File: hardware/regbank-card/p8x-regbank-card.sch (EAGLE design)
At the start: 45 parts, among them J1 DIN41612-96M, U1 P0 L0, U10 P2 L1, U11 P2 H0, U12 P2 H1, U13 P3 L0, U14 P3 L1, U15 P3 H0, U16 P3 H1, U17 PTR SEL 0, U18 PTR SEL 1, U19 PTR SEL 2, U2 P0 L1, U20 PTR SEL 3, U21 PTR SEL 4, U22 PTR SEL 5, U23 PTR SEL 6, U24 PTR SEL 7, U25 ADDR LO, U26 ADDR HI, U27 RDBK LO, U28 RDBK HI, U29 RDBK OUT, U3 P0 H0, U30 DLD DEC, U31 DOE DEC, U32 LOAD DEC, U33 SEL+CNT DEC, U34 74HCT02, U35 74HCT14, U36 ZERO P0, U37 74HCT08, U38 74HCT08, U4 P0 H1, U5 P1 L0, U6 P1 L1, U7 P1 H0, U8 P1 H1, U9 P2 L0

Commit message: hw(rev B): reg-bank — 3-bit PSEL decode + PT scratch pointer
Phase 2, step 3. Select decode U33 becomes a 74138 (3-bit PSEL -> -SEL0..4,
so PSEL=4 no longer aliases to P0); count decode moves to a new 74139
(U39, P0-P3 only). U40 (74HCT32) gates the P0-P3 load decoder off when
PSEL2=1 and derives the PT load strobes (-LDL4 = -LDL|-SEL4, etc.). PT
itself is two 74377 latches (U41/U42) loaded from D0-7, driven onto the
pointer bus by two 74244 buffers (U43/U44) when -SEL4 — so it reaches the
address bus and readback path like any pointer. Card retitled REV B.
Validates clean (pin/pad level; not yet electrically DRC'd).

Co-Authored-By: Claude Opus 4.8 <noreply@anthropic.com>
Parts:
- added U39: CNT DEC, p8x:74139
- added U40: 74HCT32, p8x:GATES14
- added U41: PT LO, p8x:74377V2
- added U42: PT HI, p8x:74377V2
- added U43: PT SEL LO, p8x:74244
- added U44: PT SEL HI, p8x:74244
- U33: value SEL+CNT DEC -> SEL DEC; device p8x:74139 -> p8x:74138
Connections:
- new net -LDH4: U40.4Y, U42.!E
- new net -LDHG: U32.!G2, U40.2Y
- new net -LDL4: U40.3Y, U41.!E
- new net -LDLG: U32.!G1, U40.1Y
- new net -SEL4: U33.Y4, U40.3B, U40.4B, U43.!G1, U43.!G2, U44.!G1, U44.!G2
- new net PSEL2: J1.C27, U33.C, U40.1B, U40.2B
- new net PTQ0_0: U41.Q1, U43.A1
- new net PTQ0_1: U41.Q2, U43.A2
- new net PTQ0_2: U41.Q3, U43.A3
- new net PTQ0_3: U41.Q4, U43.A4
- new net PTQ0_4: U41.Q5, U43.A5
- new net PTQ0_5: U41.Q6, U43.A6
- new net PTQ0_6: U41.Q7, U43.A7
- new net PTQ0_7: U41.Q8, U43.A8
- new net PTQ1_0: U42.Q1, U44.A1
- new net PTQ1_1: U42.Q2, U44.A2
- new net PTQ1_2: U42.Q3, U44.A3
- new net PTQ1_3: U42.Q4, U44.A4
- new net PTQ1_4: U42.Q5, U44.A5
- new net PTQ1_5: U42.Q6, U44.A6
- new net PTQ1_6: U42.Q7, U44.A7
- new net PTQ1_7: U42.Q8, U44.A8
- net -CNT0: now also U39.1Y0; no longer U33.2Y0
- net -CNT1: now also U39.1Y1; no longer U33.2Y1
- net -CNT2: now also U39.1Y2; no longer U33.2Y2
- net -CNT3: now also U39.1Y3; no longer U33.2Y3
- net -LDH: now also U40.2A, U40.4A; no longer U32.!G2
- net -LDL: now also U40.1A, U40.3A; no longer U32.!G1
- net -SEL0: now also U33.Y0; no longer U33.1Y0
- net -SEL1: now also U33.Y1; no longer U33.1Y1
- net -SEL2: now also U33.Y2; no longer U33.1Y2
- net -SEL3: now also U33.Y3; no longer U33.1Y3
- net CLK: now also U41.CLK, U42.CLK
- net CNTN: now also U39.!G1; no longer U33.!G2
- net D0: now also U41.D1, U42.D1
- net D1: now also U41.D2, U42.D2
- net D2: now also U41.D3, U42.D3
- net D3: now also U41.D4, U42.D4
- net D4: now also U41.D5, U42.D5
- net D5: now also U41.D6, U42.D6
- net D6: now also U41.D7, U42.D7
- net D7: now also U41.D8, U42.D8
- net GND: now also U33.!G2A, U33.!G2B, U39.A2, U39.B2; no longer U33.!G1
- net PB0: now also U43.Y1
- net PB1: now also U43.Y2
- net PB10: now also U44.Y3
- net PB11: now also U44.Y4
- net PB12: now also U44.Y5
- net PB13: now also U44.Y6
- net PB14: now also U44.Y7
- net PB15: now also U44.Y8
- net PB2: now also U43.Y3
- net PB3: now also U43.Y4
- net PB4: now also U43.Y5
- net PB5: now also U43.Y6
- net PB6: now also U43.Y7
- net PB7: now also U43.Y8
- net PB8: now also U44.Y1
- net PB9: now also U44.Y2
- net PSEL0: now also U33.A, U39.A1; no longer U33.A1, U33.A2
- net PSEL1: now also U33.B, U39.B1; no longer U33.B1, U33.B2
- net VCC: now also U33.G1, U39.!G2
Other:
- note added: "P8X REGISTER BANK CARD REV B (P0=PC P3=SP, PT scratch)"
- note removed: "P8X REGISTER BANK CARD REV A (P0=PC P3=SP)"
- moved on the sheet: LED3, LED4, LED5, R4, R5, RP1

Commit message: hw: per-IC 100nF decoupling caps on every card
card standards sec.5 requires a decoupling cap per IC; only the backplane had
them. gen_eagle's card() now generates one 100nF cap (CDn, C_DISC footprint)
per IC on the five plug-in cards, placed next to its IC and wired VCC<->GND;
the memory card's separate build does the same for U1-U9.

Caps added: control 18, regbank 44, alu 31, io 15, cf 8, memory 9. All 7
boards regenerate with 0 validation errors; card schematic PDFs refreshed.
Placement is approximate (caps sit just below each IC) pending Fusion routing.

Clears a pre-fab blocker from the backlog.

Co-Authored-By: Claude Opus 4.8 <noreply@anthropic.com>
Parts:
- added CD1, CD10, CD11, CD12, CD13, CD14, CD15, CD16, CD17, CD18, CD19, CD2, CD20, CD21, CD22, CD23, CD24, CD25, CD26, CD27, CD28, CD29, CD3, CD30, CD31, CD32, CD33, CD34, CD35, CD36, CD37, CD38, CD39, CD4, CD40, CD41, CD42, CD43, CD44, CD5, CD6, CD7, CD8, CD9: 100N, p8x:CAP
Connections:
- net GND: now also CD1.2, CD10.2, CD11.2, CD12.2, CD13.2, CD14.2, CD15.2, CD16.2, CD17.2, CD18.2, CD19.2, CD2.2, CD20.2, CD21.2, CD22.2, CD23.2, CD24.2, CD25.2, CD26.2, CD27.2, CD28.2, CD29.2, CD3.2, CD30.2, CD31.2, CD32.2, CD33.2, CD34.2, CD35.2, CD36.2, CD37.2, CD38.2, CD39.2, CD4.2, CD40.2, CD41.2, CD42.2, CD43.2, CD44.2, CD5.2, CD6.2, CD7.2, CD8.2, CD9.2
- net VCC: now also CD1.1, CD10.1, CD11.1, CD12.1, CD13.1, CD14.1, CD15.1, CD16.1, CD17.1, CD18.1, CD19.1, CD2.1, CD20.1, CD21.1, CD22.1, CD23.1, CD24.1, CD25.1, CD26.1, CD27.1, CD28.1, CD29.1, CD3.1, CD30.1, CD31.1, CD32.1, CD33.1, CD34.1, CD35.1, CD36.1, CD37.1, CD38.1, CD39.1, CD4.1, CD40.1, CD41.1, CD42.1, CD43.1, CD44.1, CD5.1, CD6.1, CD7.1, CD8.1, CD9.1

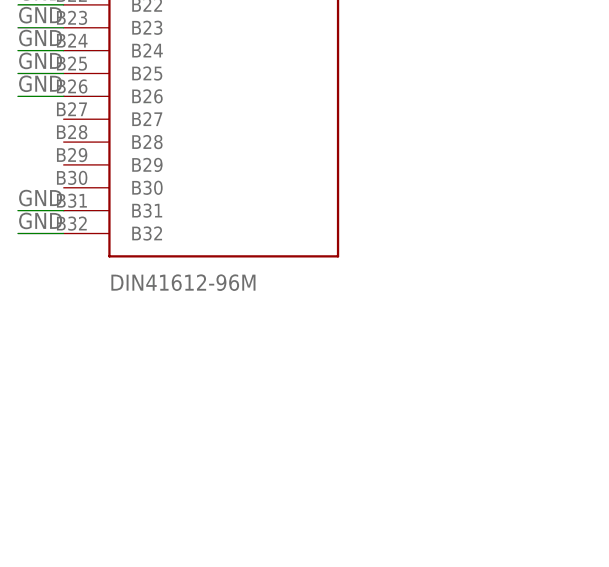
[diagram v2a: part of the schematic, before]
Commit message: fix(bom): card DIN connectors were undercounted (1 -> 6); label them FABC96R
Two fixes:
- card() built CARDS[name] from `allp`, which omitted J1 — so the 5 plug-in
  cards' DIN41612 edge connectors never reached the BOM (it showed qty 1, only
  the memory card's J1). Include J1 in allp (the schematic renderer already
  filters J1 by name, so rendering is unchanged). BOM now correctly shows 6 card
  connectors + 10 backplane receptacles.
- Card edge connector is FABC96R (user-specified): set the value label on every
  card J1 and name it in the BOM; backplane receptacles noted as the mating part.

Regenerated all boards + PDFs + BOM; all 6 test suites pass.

Co-Authored-By: Claude Opus 4.8 <noreply@anthropic.com>
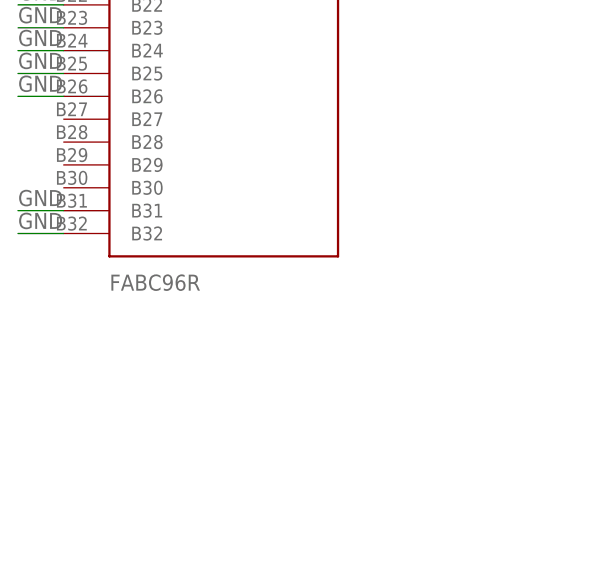
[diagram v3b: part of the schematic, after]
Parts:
- J1: value DIN41612-96M -> FABC96R
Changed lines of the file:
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@@
 <classes><class number="0" name="default" width="0" drill="0"/></classes>
 <parts>
-<part name="J1" library="p8x" deviceset="DIN96" device="" value="DIN41612-96M"/>
+<part name="J1" library="p8x" deviceset="DIN96" device="" value="FABC96R"/>
 <part name="U1" library="p8x" deviceset="74169" device="" value="P0 L0"/>
 <part name="U2" library="p8x" deviceset="74169" device="" value="P0 L1"/>

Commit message: fix(hardware): connect IC power pins on the card()-built boards
Schematic-review fix. card() wired the edge-connector and decoupling-cap pins to
VCC/GND but never added each IC's own VCC/GND supply pin, so on control, regbank,
ALU, I/O, and CF the chips' power pads were not members of the power pours and
would not have been powered. (The hand-built memory card already did this; the
backplane has no ICs. validate() couldn't catch it — it checks pin-name legality,
not connectivity.)

- card(): append (ref,"VCC")/(ref,"GND") for every IC, skipping any pin already
  wired by hand (idempotent — avoids duplicate pinrefs, e.g. ALU U16 GND)
- regenerated all 7 boards (.sch/.brd), 0 validation errors
- board-level audit: every IC on every card now has both VCC and GND on the
  power signals
- BACKLOG: moved the critical item to DONE; theory docs' power-pin callouts
  updated to "fixed"

Co-Authored-By: Claude Opus 4.8 <noreply@anthropic.com>
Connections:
- net GND: now also U1.GND, U10.GND, U11.GND, U12.GND, U13.GND, U14.GND, U15.GND, U16.GND, U17.GND, U18.GND, U19.GND, U2.GND, U20.GND, U21.GND, U22.GND, U23.GND, U24.GND, U25.GND, U26.GND, U27.GND, U28.GND, U29.GND, U3.GND, U30.GND, U31.GND, U32.GND, U33.GND, U34.GND, U35.GND, U36.GND, U37.GND, U38.GND, U39.GND, U4.GND, U40.GND, U41.GND, U42.GND, U43.GND, U44.GND, U5.GND, U6.GND, U7.GND, U8.GND, U9.GND
- net VCC: now also U1.VCC, U10.VCC, U11.VCC, U12.VCC, U13.VCC, U14.VCC, U15.VCC, U16.VCC, U17.VCC, U18.VCC, U19.VCC, U2.VCC, U20.VCC, U21.VCC, U22.VCC, U23.VCC, U24.VCC, U25.VCC, U26.VCC, U27.VCC, U28.VCC, U29.VCC, U3.VCC, U30.VCC, U31.VCC, U32.VCC, U33.VCC, U34.VCC, U35.VCC, U36.VCC, U37.VCC, U38.VCC, U39.VCC, U4.VCC, U40.VCC, U41.VCC, U42.VCC, U43.VCC, U44.VCC, U5.VCC, U6.VCC, U7.VCC, U8.VCC, U9.VCC

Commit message: feat(backplane): row-B even pins become spare bus lines (SPARE12-23)
Row B was a solid ground guard (B3-26 all GND). Per request, B3-26 now ALTERNATE:
odd pins stay GND (still a guard between most signal pairs), and the 12 even pins
(B4,B6,..,B26) become spare bus lines SPARE12-SPARE23, routed slot-to-slot — so
new signals can be added later without re-spinning the backplane. B27-30
(CLRC/BSEL/IRQ/SPARE11) unchanged.

- busnet() updated in all three copies (gen_eagle, gen_bus_pdf, gen_bus_card)
- backplane .brd routes the 12 new spares (mirrors the B27-30 routing); odd-pin
  grounds remain on the GND pour
- every card regenerated: their connectors no longer tie the even B pins to GND
  (those are spare lines now) — they simply don't connect the spares
- all 8 boards validate (0 errors); schematic + bus PDFs regenerated
- docs updated: bus-definition (pin map + notes), backplane theory + design notes
- net signal-integrity trade noted: a solid guard shields slightly better; the
  alternation was chosen deliberately for expansion room

Co-Authored-By: Claude Opus 4.8 <noreply@anthropic.com>
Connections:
- net GND: no longer J1.B10, J1.B12, J1.B14, J1.B16, J1.B18, J1.B20, J1.B22, J1.B24, J1.B26, J1.B4, J1.B6, J1.B8
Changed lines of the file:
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@@
 <wire x1="-17.78" y1="-48.26" x2="-22.86" y2="-48.26" width="0.1524" layer="91"/>
 <label x="-22.86" y="-47.75" size="1.778" layer="95"/></segment>
-<segment><pinref part="J1" gate="G$1" pin="B4"/>
-<wire x1="-17.78" y1="-50.80" x2="-22.86" y2="-50.80" width="0.1524" layer="91"/>
-<label x="-22.86" y="-50.29" size="1.778" layer="95"/></segment>
 <segment><pinref part="J1" gate="G$1" pin="B5"/>
 <wire x1="-17.78" y1="-53.34" x2="-22.86" y2="-53.34" width="0.1524" layer="91"/>
 <label x="-22.86" y="-52.83" size="1.778" layer="95"/></segment>
-<segment><pinref part="J1" gate="G$1" pin="B6"/>
-<wire x1="-17.78" y1="-55.88" x2="-22.86" y2="-55.88" width="0.1524" layer="91"/>
-<label x="-22.86" y="-55.37" size="1.778" layer="95"/></segment>
 <segment><pinref part="J1" gate="G$1" pin="B7"/>
 <wire x1="-17.78" y1="-58.42" x2="-22.86" y2="-58.42" width="0.1524" layer="91"/>
 <label x="-22.86" y="-57.91" size="1.778" layer="95"/></segment>
-<segment><pinref part="J1" gate="G$1" pin="B8"/>
-<wire x1="-17.78" y1="-60.96" x2="-22.86" y2="-60.96" width="0.1524" layer="91"/>
-<label x="-22.86" y="-60.45" size="1.778" layer="95"/></segment>
 <segment><pinref part="J1" gate="G$1" pin="B9"/>
 <wire x1="-17.78" y1="-63.50" x2="-22.86" y2="-63.50" width="0.1524" layer="91"/>
 <label x="-22.86" y="-62.99" size="1.778" layer="95"/></segment>
-<segment><pinref part="J1" gate="G$1" pin="B10"/>
-<wire x1="-17.78" y1="-66.04" x2="-22.86" y2="-66.04" width="0.1524" layer="91"/>
-<label x="-22.86" y="-65.53" size="1.778" layer="95"/></segment>
 <segment><pinref part="J1" gate="G$1" pin="B11"/>
 <wire x1="-17.78" y1="-68.58" x2="-22.86" y2="-68.58" width="0.1524" layer="91"/>
 <label x="-22.86" y="-68.07" size="1.778" layer="95"/></segment>
-<segment><pinref part="J1" gate="G$1" pin="B12"/>
-<wire x1="-17.78" y1="-71.12" x2="-22.86" y2="-71.12" width="0.1524" layer="91"/>
-<label x="-22.86" y="-70.61" size="1.778" layer="95"/></segment>
 <segment><pinref part="J1" gate="G$1" pin="B13"/>
 <wire x1="-17.78" y1="-73.66" x2="-22.86" y2="-73.66" width="0.1524" layer="91"/>
 <label x="-22.86" y="-73.15" size="1.778" layer="95"/></segment>
-<segment><pinref part="J1" gate="G$1" pin="B14"/>
-<wire x1="-17.78" y1="-76.20" x2="-22.86" y2="-76.20" width="0.1524" layer="91"/>
-<label x="-22.86" y="-75.69" size="1.778" layer="95"/></segment>
 <segment><pinref part="J1" gate="G$1" pin="B15"/>
 <wire x1="-17.78" y1="-78.74" x2="-22.86" y2="-78.74" width="0.1524" layer="91"/>
 <label x="-22.86" y="-78.23" size="1.778" layer="95"/></segment>
-<segment><pinref part="J1" gate="G$1" pin="B16"/>
-<wire x1="-17.78" y1="-81.28" x2="-22.86" y2="-81.28" width="0.1524" layer="91"/>
-<label x="-22.86" y="-80.77" size="1.778" layer="95"/></segment>
 <segment><pinref part="J1" gate="G$1" pin="B17"/>
 <wire x1="-17.78" y1="-83.82" x2="-22.86" y2="-83.82" width="0.1524" layer="91"/>
 <label x="-22.86" y="-83.31" size="1.778" layer="95"/></segment>
-<segment><pinref part="J1" gate="G$1" pin="B18"/>
-<wire x1="-17.78" y1="-86.36" x2="-22.86" y2="-86.36" width="0.1524" layer="91"/>
-<label x="-22.86" y="-85.85" size="1.778" layer="95"/></segment>
 <segment><pinref part="J1" gate="G$1" pin="B19"/>
 <wire x1="-17.78" y1="-88.90" x2="-22.86" y2="-88.90" width="0.1524" layer="91"/>
 <label x="-22.86" y="-88.39" size="1.778" layer="95"/></segment>
-<segment><pinref part="J1" gate="G$1" pin="B20"/>
-<wire x1="-17.78" y1="-91.44" x2="-22.86" y2="-91.44" width="0.1524" layer="91"/>
-<label x="-22.86" y="-90.93" size="1.778" layer="95"/></segment>
 <segment><pinref part="J1" gate="G$1" pin="B21"/>
 <wire x1="-17.78" y1="-93.98" x2="-22.86" y2="-93.98" width="0.1524" layer="91"/>
 <label x="-22.86" y="-93.47" size="1.778" layer="95"/></segment>
-<segment><pinref part="J1" gate="G$1" pin="B22"/>
-<wire x1="-17.78" y1="-96.52" x2="-22.86" y2="-96.52" width="0.1524" layer="91"/>
-<label x="-22.86" y="-96.01" size="1.778" layer="95"/></segment>
 <segment><pinref part="J1" gate="G$1" pin="B23"/>
 <wire x1="-17.78" y1="-99.06" x2="-22.86" y2="-99.06" width="0.1524" layer="91"/>
 <label x="-22.86" y="-98.55" size="1.778" layer="95"/></segment>
-<segment><pinref part="J1" gate="G$1" pin="B24"/>
-<wire x1="-17.78" y1="-101.60" x2="-22.86" y2="-101.60" width="0.1524" layer="91"/>
-<label x="-22.86" y="-101.09" size="1.778" layer="95"/></segment>
 <segment><pinref part="J1" gate="G$1" pin="B25"/>
 <wire x1="-17.78" y1="-104.14" x2="-22.86" y2="-104.14" width="0.1524" layer="91"/>
 <label x="-22.86" y="-103.63" size="1.778" layer="95"/></segment>
-<segment><pinref part="J1" gate="G$1" pin="B26"/>
-<wire x1="-17.78" y1="-106.68" x2="-22.86" y2="-106.68" width="0.1524" layer="91"/>
-<label x="-22.86" y="-106.17" size="1.778" layer="95"/></segment>
 <segment><pinref part="J1" gate="G$1" pin="B31"/>
 <wire x1="-17.78" y1="-119.38" x2="-22.86" y2="-119.38" width="0.1524" layer="91"/>

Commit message: feat(generators): roll out part-number values + function labels to all cards
Apply the value=part-number / function-as-label convention across every card
(was proven on the LED card). A device->part-number map (PN) + a small resolver
in card() do it automatically:

- logic/memory ICs -> generic type numbers (74HCT138, 74HCT244, 28C64, 6850,
  MAX232, ...); the old per-part function text becomes the placed schematic label
- LEDs -> value = colour (GRN/YEL/RED), function -> label (POWER, RUN, HALT, ...)
- switches -> SPST, function -> label (RUN/HALT, STEP, RESET)
- headers -> 1x3 / 1x4, function -> label (CLKSEL, RTC 3-WIRE, SERIAL)
- gate arrays / passives / connectors keep their value (74HCT08, 1K, 100N,
  FABC96R, 28C256, 62256, IDE-40); a few contaminated values hand-cleaned
  (gate-array suffixes, IDE label) with explicit labels where meaningful

Net result: the Eagle `value` field is a clean orderable part number everywhere
(BOM + >VALUE + board silk), and the logical function is placed text near each
chip. Regenerated all boards + schematic PDFs; all 8 validate (0 errors).

Co-Authored-By: Claude Opus 4.8 <noreply@anthropic.com>
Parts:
- LED3: value PWR-GRN -> GRN
- LED4: value RD-GRN -> GRN
- LED5: value LD-YEL -> YEL
- U1: value P0 L0 -> 74HCT169
- U10: value P2 L1 -> 74HCT169
- U11: value P2 H0 -> 74HCT169
- U12: value P2 H1 -> 74HCT169
- U13: value P3 L0 -> 74HCT169
- U14: value P3 L1 -> 74HCT169
- U15: value P3 H0 -> 74HCT169
- U16: value P3 H1 -> 74HCT169
- U17: value PTR SEL 0 -> 74HCT244
- U18: value PTR SEL 1 -> 74HCT244
- U19: value PTR SEL 2 -> 74HCT244
- U2: value P0 L1 -> 74HCT169
- U20: value PTR SEL 3 -> 74HCT244
- U21: value PTR SEL 4 -> 74HCT244
- U22: value PTR SEL 5 -> 74HCT244
- U23: value PTR SEL 6 -> 74HCT244
- U24: value PTR SEL 7 -> 74HCT244
- U25: value ADDR LO -> 74HCT244
- U26: value ADDR HI -> 74HCT244
- U27: value RDBK LO -> 74HCT257
- U28: value RDBK HI -> 74HCT257
- U29: value RDBK OUT -> 74HCT244
- U3: value P0 H0 -> 74HCT169
- U30: value DLD DEC -> 74HCT138
- U31: value DOE DEC -> 74HCT138
- U32: value LOAD DEC -> 74HCT139
- U33: value SEL DEC -> 74HCT138
- U36: value ZERO P0 -> 74HCT244
- U39: value CNT DEC -> 74HCT139
- U4: value P0 H1 -> 74HCT169
- U41: value PT LO -> 74HCT377
- U42: value PT HI -> 74HCT377
- U43: value PT SEL LO -> 74HCT244
- U44: value PT SEL HI -> 74HCT244
- U5: value P1 L0 -> 74HCT169
- U6: value P1 L1 -> 74HCT169
- U7: value P1 H0 -> 74HCT169
- U8: value P1 H1 -> 74HCT169
- U9: value P2 L0 -> 74HCT169
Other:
- note added: "74HCT138"
- note added: "74HCT139"
- note added: "74HCT169"
- note added: "74HCT244"
- note added: "74HCT257"
- note added: "74HCT377"
- note added: "ADDR HI"
- note added: "ADDR LO"
- note added: "CNT DEC"
- note added: "DLD DEC"
- note added: "DOE DEC"
- note added: "GRN"
- note added: "LD"
- note added: "LOAD DEC"
- note added: "P0 H0"
- note added: "P0 H1"
- note added: "P0 L0"
- note added: "P0 L1"
- note added: "P1 H0"
- note added: "P1 H1"
- note added: "P1 L0"
- note added: "P1 L1"
- note added: "P2 H0"
- note added: "P2 H1"
- note added: "P2 L0"
- note added: "P2 L1"
- note added: "P3 H0"
- note added: "P3 H1"
- note added: "P3 L0"
- note added: "P3 L1"
- note added: "PT HI"
- note added: "PT LO"
- note added: "PT SEL HI"
- note added: "PT SEL LO"
- note added: "PTR SEL 0"
- note added: "PTR SEL 1"
- note added: "PTR SEL 2"
- note added: "PTR SEL 3"
- note added: "PTR SEL 4"
- note added: "PTR SEL 5"
- note added: "PTR SEL 6"
- note added: "PTR SEL 7"
- note added: "PWR"
- note added: "RD"
- note added: "RDBK HI"
- note added: "RDBK LO"
- note added: "RDBK OUT"
- note added: "SEL DEC"
- note added: "YEL"
- note added: "ZERO P0"

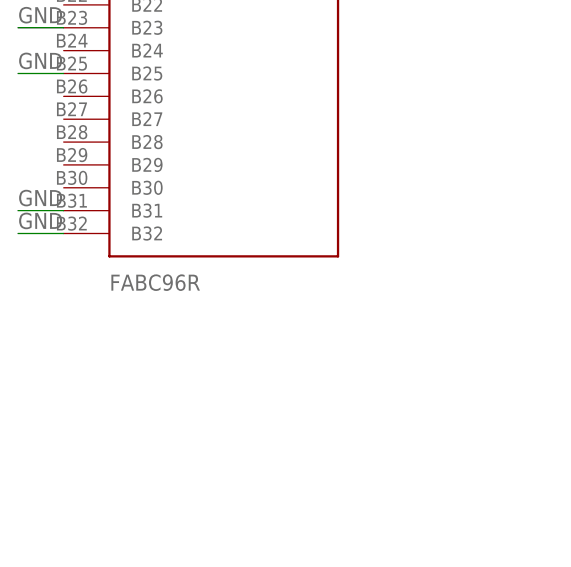
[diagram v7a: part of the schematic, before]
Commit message: feat(hardware): use con-vg DIN 41612 footprints (MABC96R card / FABC96S backplane)
Replace the hand-rolled DIN96/DIN96C connector packages with the real Eagle
con-vg DIN 41612 footprints (geometry baked into the generator so it stays
self-contained): card edge = MABC96R (male right-angle), backplane = FABC96S
(female vertical) — both A/B/C @ 2.54mm, drill 0.9144, two M2.5 mounting holes
at y=+/-45. Card value -> MABC96R; pin->pad names unchanged (A1..C32) so the
netlist is intact.

con-vg centres the pad field on the element origin, so the backplane (hand-
placed/routed) was re-derived: slots dropped to y=54.6 to centre the pin field
on the 109mm board (pads now on-board), bus traces re-routed to the new A/B/C
columns (element at sx(i)-2.54). Cards auto-adapt via fp_box. All 8 boards
validate (0 errors).

Known: 3 placement-overlap WARNINGS on the backplane (power-LED resistor; CT2/RT1
clock terminators, both DNP) where the taller connector crowds the top/bottom
strips — to clear during the Fusion placement pass.

Co-Authored-By: Claude Opus 4.8 <noreply@anthropic.com>
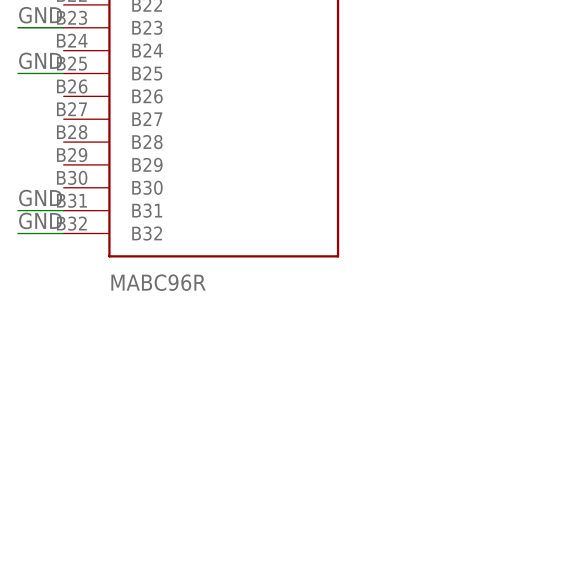
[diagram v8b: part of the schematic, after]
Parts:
- J1: value FABC96R -> MABC96R
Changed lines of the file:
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@@
 <classes><class number="0" name="default" width="0" drill="0"/></classes>
 <parts>
-<part name="J1" library="p8x" deviceset="DIN96" device="" value="FABC96R"/>
+<part name="J1" library="p8x" deviceset="DIN96" device="" value="MABC96R"/>
 <part name="U1" library="p8x" deviceset="74169" device="" value="74HCT169"/>
 <part name="U2" library="p8x" deviceset="74169" device="" value="74HCT169"/>
